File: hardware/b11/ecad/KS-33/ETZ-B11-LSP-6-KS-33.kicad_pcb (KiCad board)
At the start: 2 copper layers, 163.9 x 90.2 mm, 3 parts

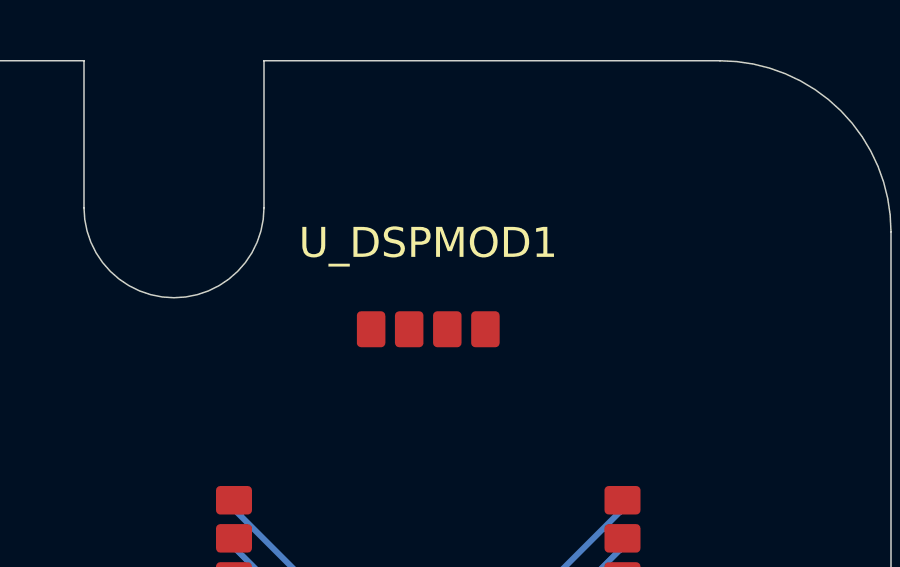
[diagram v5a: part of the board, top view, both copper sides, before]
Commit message: feat: add B11 buzzer footprint [skip ci]
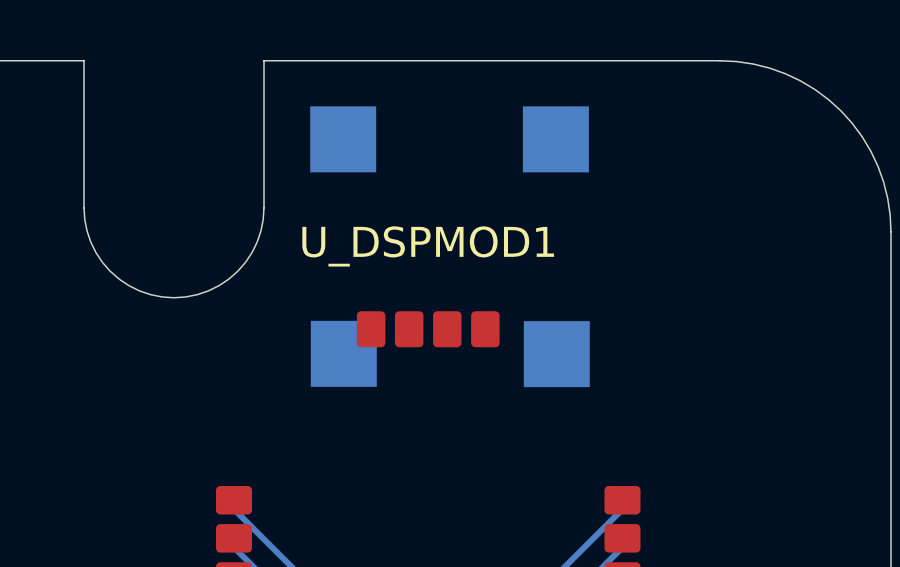
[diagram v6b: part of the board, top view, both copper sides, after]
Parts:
- added BZ1: KLJ-8530-3627, KLJ-8530-3627, B.Cu at (215.7, 65.4)

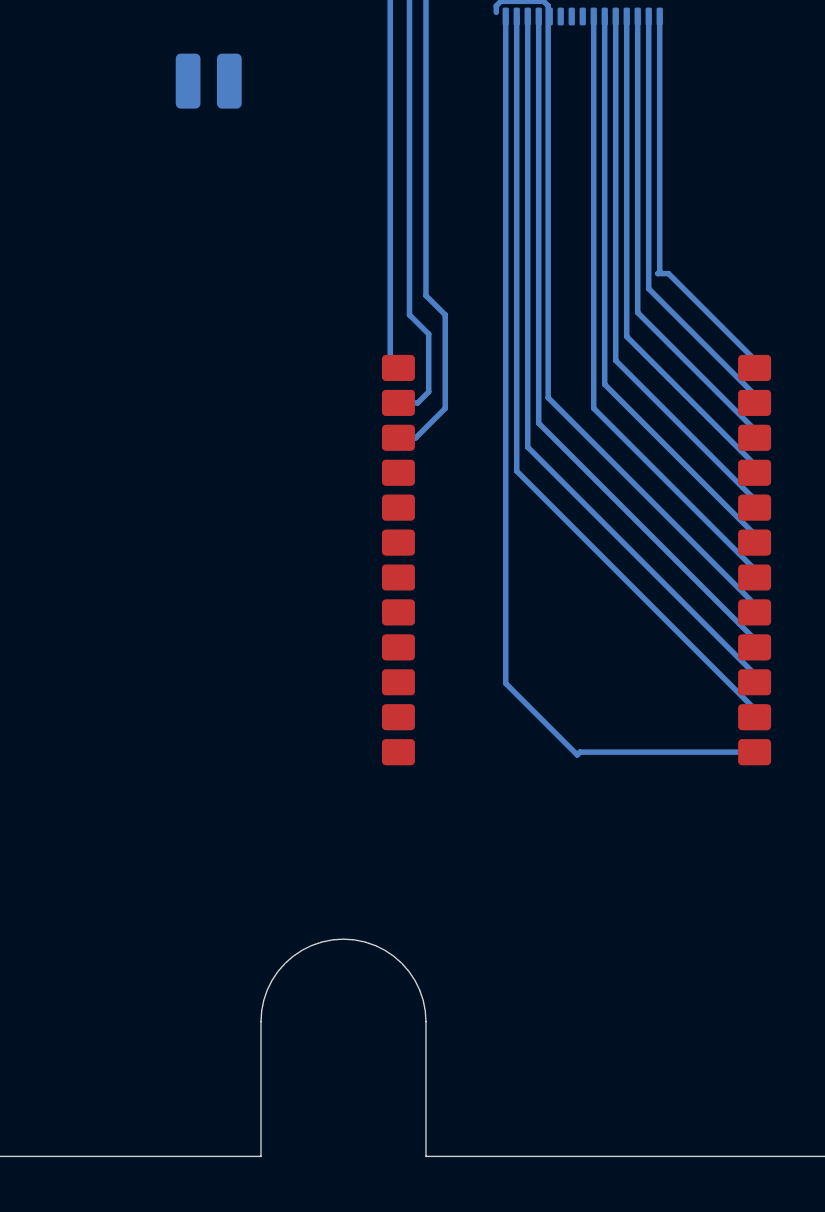
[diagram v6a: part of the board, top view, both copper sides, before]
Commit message: feat: add B11 haptic and pogo connector assets [skip ci]
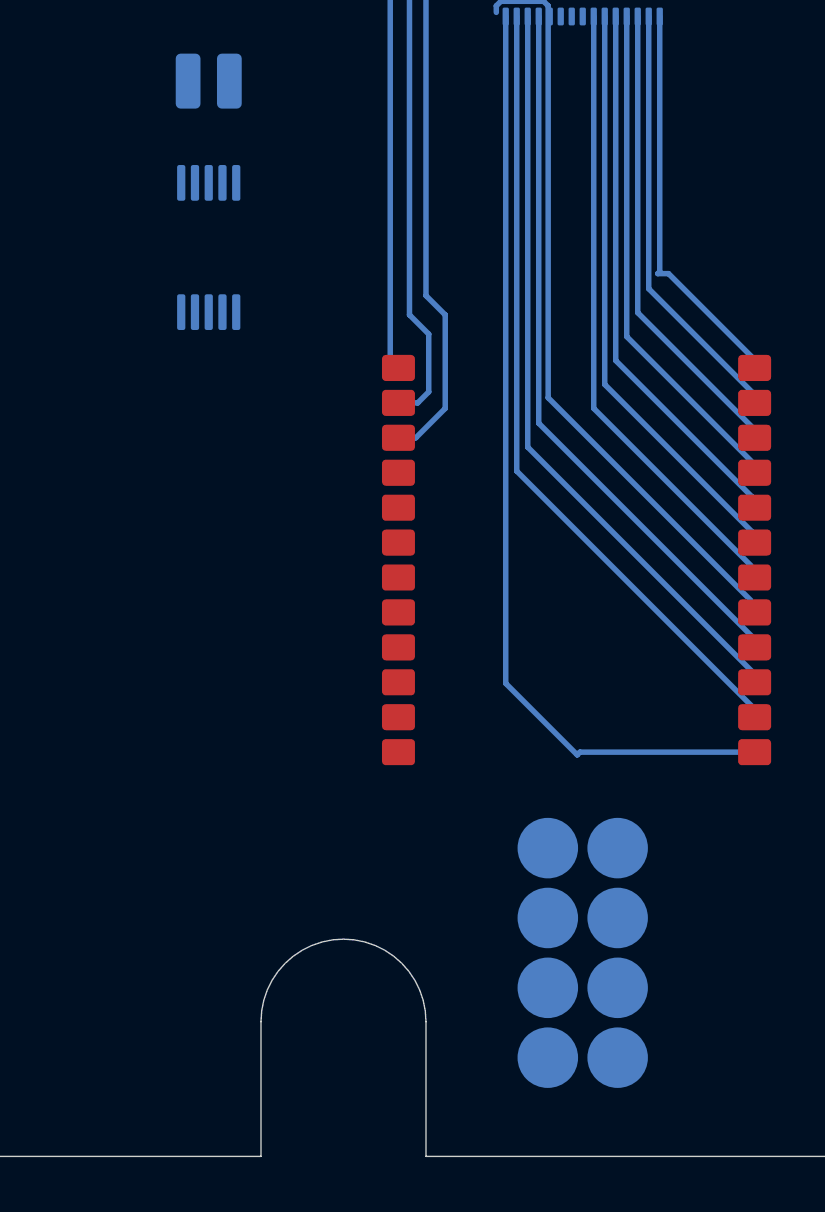
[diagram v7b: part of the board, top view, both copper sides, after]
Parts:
- added J_LOGIC1: POGO-PADS-2X4-P2.54, POGO-PADS-2X4-P2.54, B.Cu at (215.2, 142.0)
- added U_HAPTIC1: DRV2605LDGSR, DRV2605LDGSR, B.Cu at (201.7, 116.3)

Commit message: feat: add B11 buzzer h-bridge driver [skip ci]
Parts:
- added U_BUZZ1: DRV8837DSGR, DRV8837DSGR, B.Cu at (215.8, 73.1)
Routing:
- net LED_CS4: track 29.2 -> 34.3 mm
- net LED_CS3: track 27.8 -> 32.6 mm
- net LED_CS2: track 26.3 -> 31.0 mm
- net LED_SW7: track 22.9 -> 26.3 mm
- net LED_SW6: track 21.5 -> 24.7 mm
- net LED_SW5: track 20.1 -> 23.0 mm
- net LED_SW4: track 18.6 -> 21.3 mm
- net LED_SW3: track 17.2 -> 19.7 mm
- net LED_SW2: track 15.8 -> 18.0 mm
- net LED_CS1: track 27.6 -> 29.3 mm
- net LED_SW1: track 14.6 -> 16.2 mm
- net LED_CS18: track 15.8 -> 17.2 mm
- net LED_CS5: track 34.7 -> 35.9 mm
- net LED_CS15: track 23.2 -> 24.2 mm
- net LED_CS16: track 22.7 -> 23.5 mm
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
